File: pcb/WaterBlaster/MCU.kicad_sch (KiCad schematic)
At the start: 13 parts, among them J11 Conn_01x03, J12 Conn_01x03, J2 JTAG_Header, J4 Conn_01x02, J4 WaterBlaster:MOLEX_436500227, SW6 SW_Push, U3 STM32G070KBT6

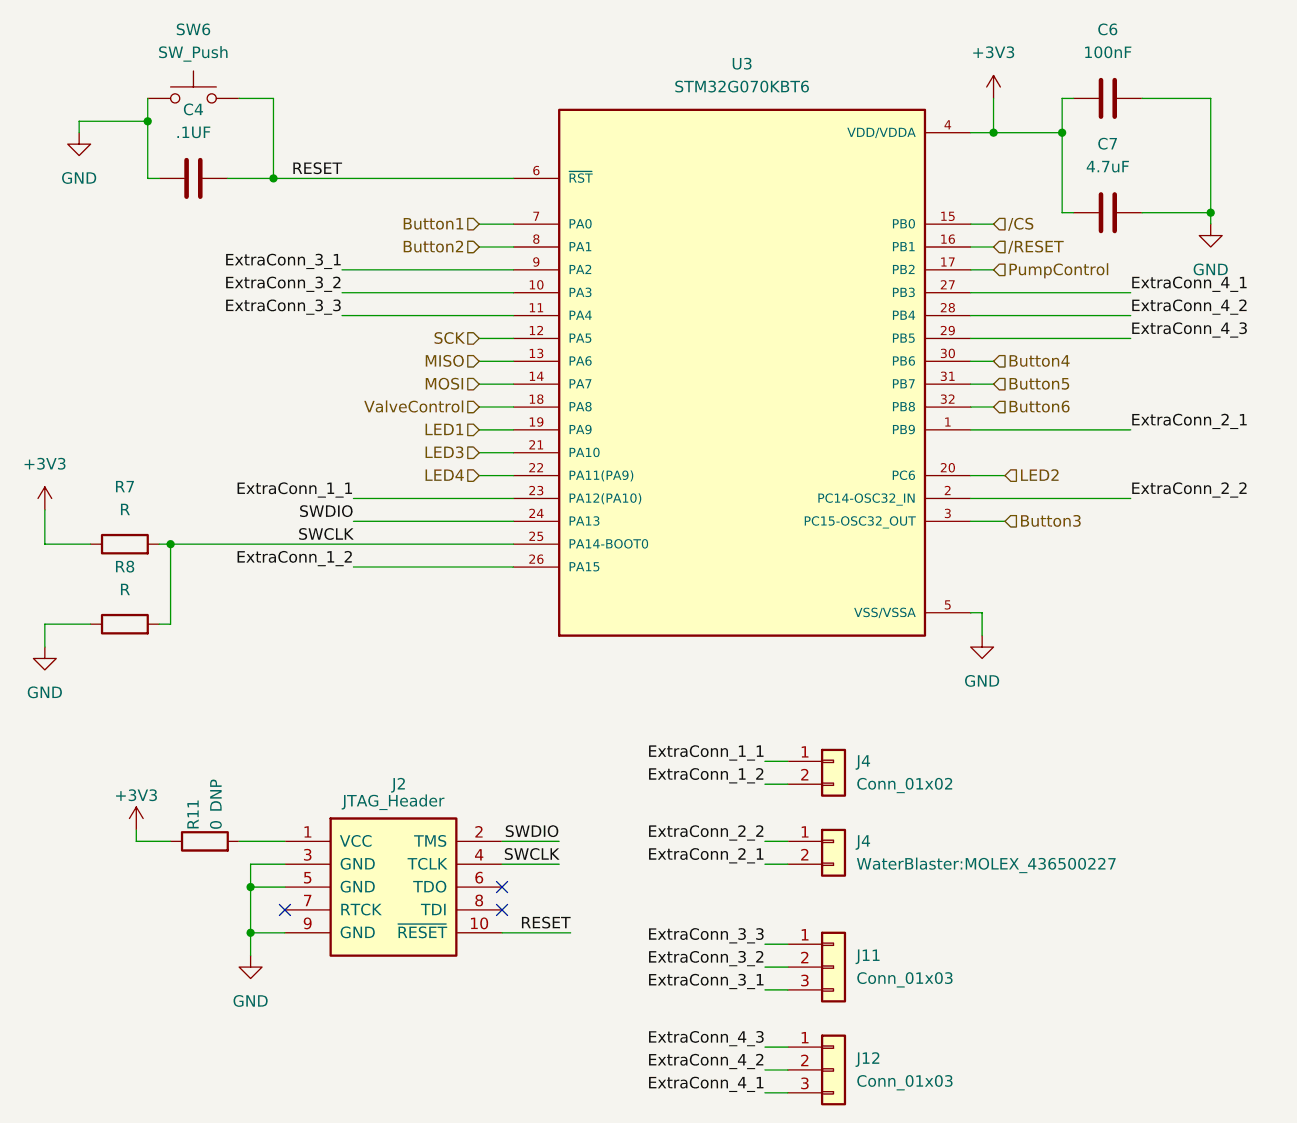
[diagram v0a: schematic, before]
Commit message: Updating firmware and CAD
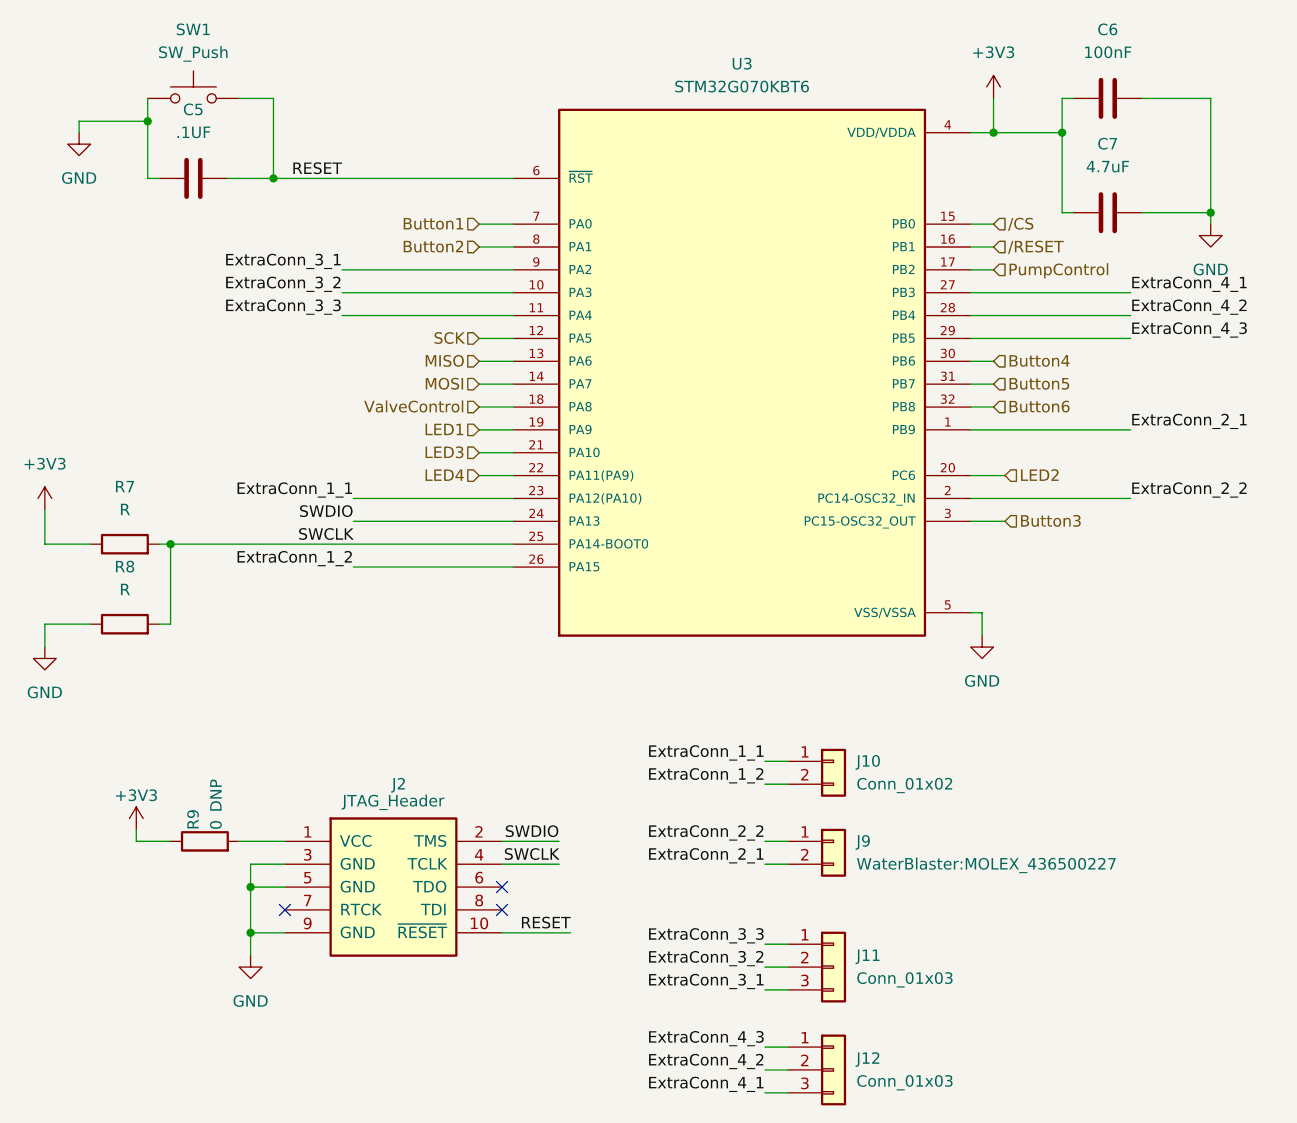
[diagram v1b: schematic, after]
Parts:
- R9: renamed from R11; value 0 -> 0
- renumbered C4 to C5, J4 to J10, J4 to J9, SW6 to SW1
